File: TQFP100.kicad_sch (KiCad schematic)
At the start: 5 parts, among them IC1 100-PQFP, J1 Conn_02x15_Counter_Clockwise, J2 Conn_02x10_Odd_Even_MountingP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, J3 Conn_02x15_Counter_Clockwise, J4 Conn_02x10_Odd_Even_MountingP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

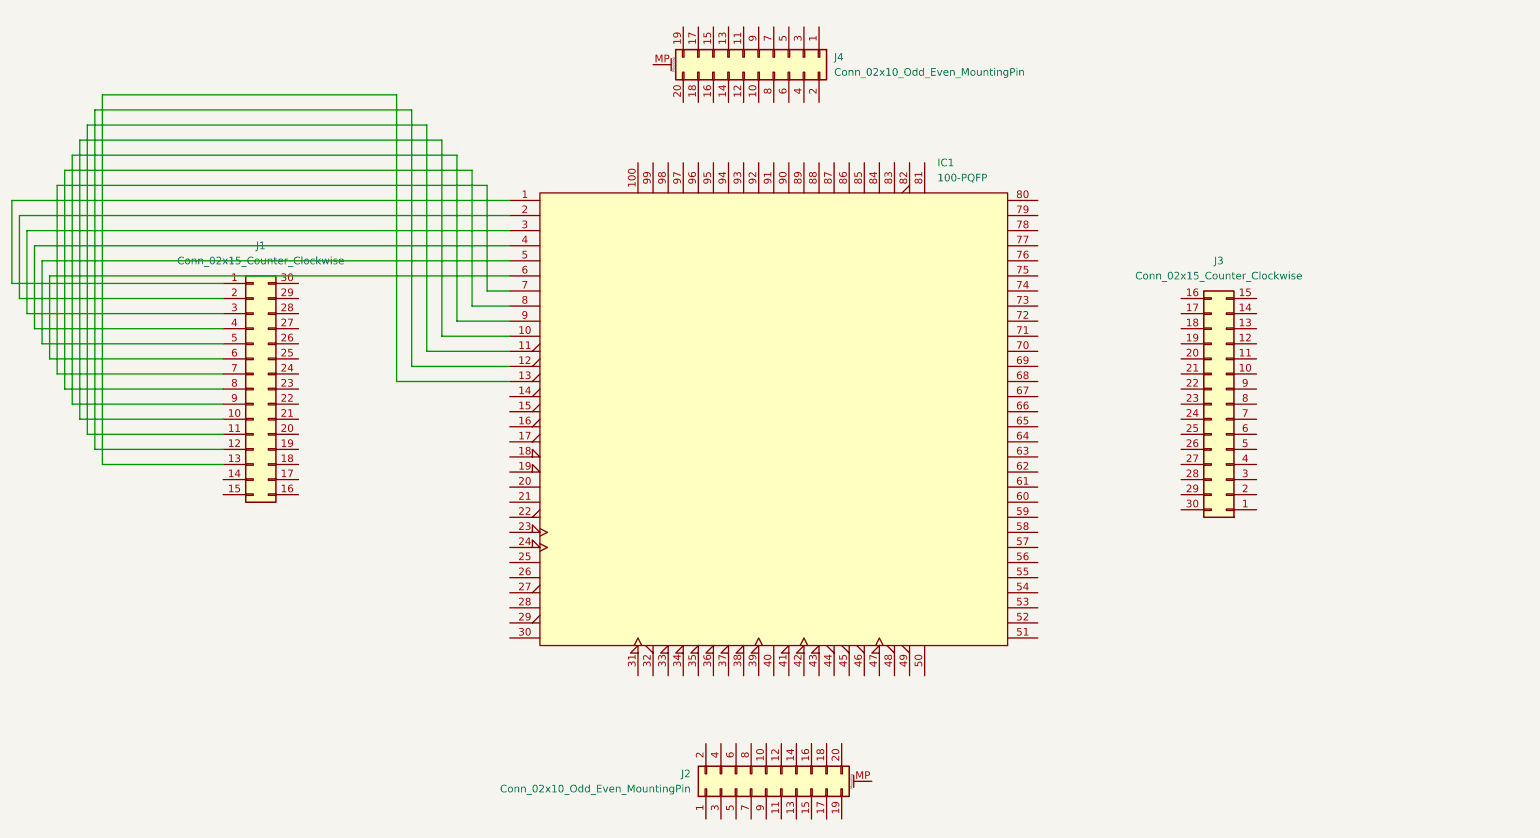
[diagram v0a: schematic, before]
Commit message: Corrected pinheader size
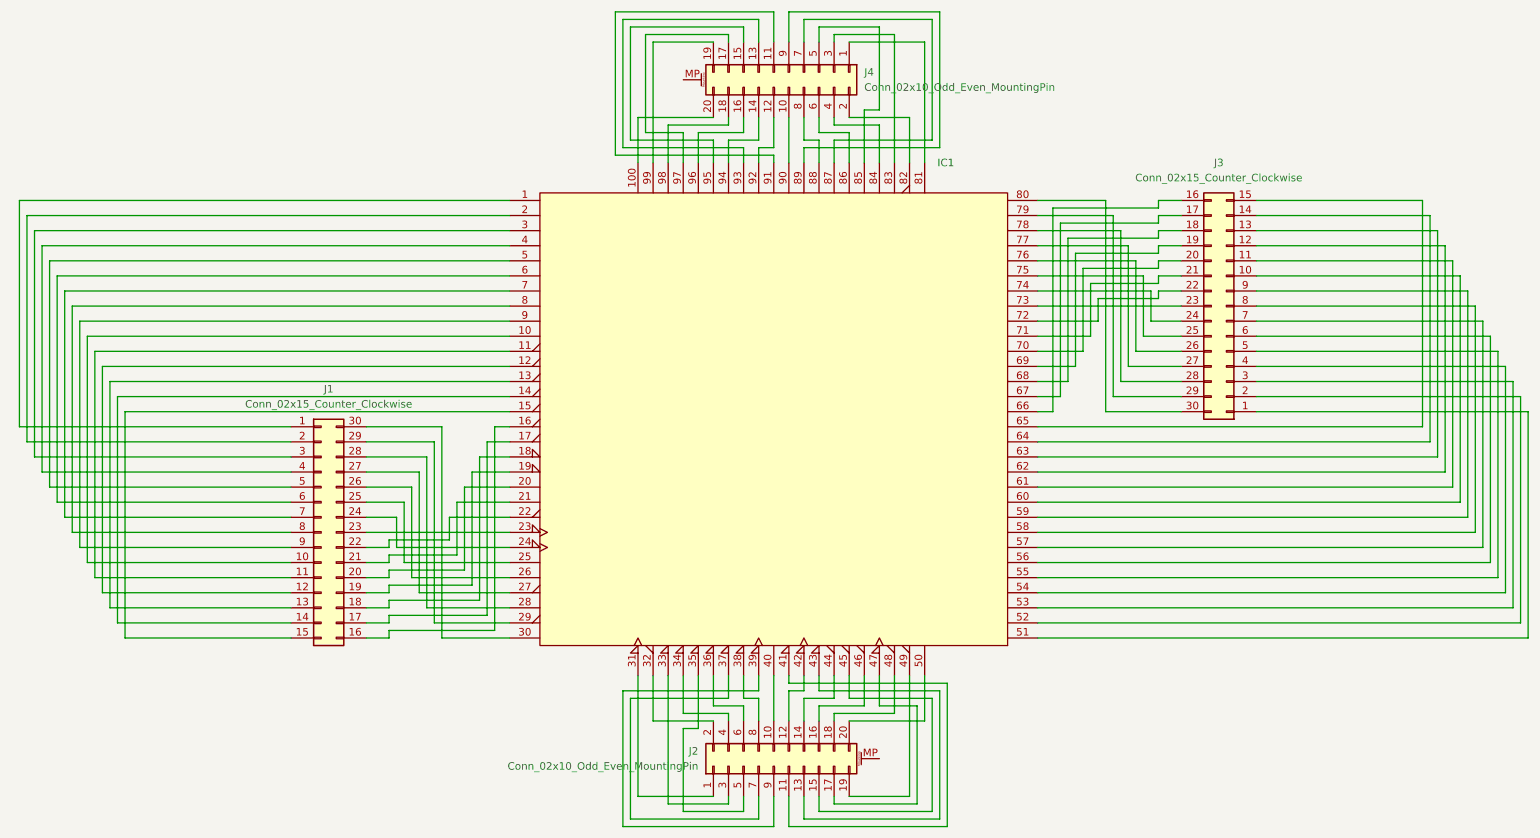
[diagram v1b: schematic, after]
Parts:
- J1, J3: footprint Connector_PinHeader_1.00mm:PinHeader_2x15_P1.00mm_Vertical -> Connector_PinHeader_2.54mm:PinHeader_2x15_P2.54mm_Vertical
- J2, J4: footprint Connector_PinHeader_1.00mm:PinHeader_2x10_P1.00mm_Vertical -> Connector_PinHeader_2.54mm:PinHeader_2x10_P2.54mm_Vertical
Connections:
- net at J4.1 (Pin_1): now also IC1.81 (A22)
- net at J4.10 (Pin_10): now also IC1.90 (VDD_8)
- net at J4.11 (Pin_11): now also IC1.91 (A15)
- net at J4.12 (Pin_12): now also IC1.92 (A14)
- net at J4.13 (Pin_13): now also IC1.93 (A13)
- net at J4.14 (Pin_14): now also IC1.94 (A12)
- net at J4.15 (Pin_15): now also IC1.95 (A11)
- net at J4.16 (Pin_16): now also IC1.96 (A10)
- net at J4.17 (Pin_17): now also IC1.97 (A09)
- net at J4.18 (Pin_18): now also IC1.98 (A08)
- net at J4.19 (Pin_19): now also IC1.99 (A07)
- net at J4.2 (Pin_2): now also IC1.82 (A21)
- net at J4.20 (Pin_20): now also IC1.100 (A06)
- net at J4.3 (Pin_3): now also IC1.83 (A20)
- net at J4.4 (Pin_4): now also IC1.84 (A19)
- net at J4.5 (Pin_5): now also IC1.85 (A18)
- net at J4.6 (Pin_6): now also IC1.86 (A17)
- net at J4.7 (Pin_7): now also IC1.87 (A16)
- net at J4.8 (Pin_8): now also IC1.88 (VDD_7)
- net at J4.9 (Pin_9): now also IC1.89 (VSS_8)
- net at J2.1 (Pin_1): now also IC1.31 (~{INTAK})
- net at J2.10 (Pin_10): now also IC1.40 (CLKSEL)
- net at J2.11 (Pin_11): now also IC1.41 (~{HALT})
- net at J2.12 (Pin_12): now also IC1.42 (~{STNBY})
- net at J2.13 (Pin_13): now also IC1.43 (~{EV})
- net at J2.14 (Pin_14): now also IC1.44 (~{UMCS})
- net at J2.15 (Pin_15): now also IC1.45 (~{MCS3})
- net at J2.16 (Pin_16): now also IC1.46 (~{MCS2})
- net at J2.17 (Pin_17): now also IC1.47 (~{MCS1})
- net at J2.18 (Pin_18): now also IC1.48 (~{MCS0})
- net at J2.19 (Pin_19): now also IC1.49 (~{LMCS})
- net at J2.2 (Pin_2): now also IC1.32 (~{BACK})
- net at J2.20 (Pin_20): now also IC1.50 (VDD_4)
- net at J2.3 (Pin_3): now also IC1.33 (~{BREQ})
- net at J2.4 (Pin_4): now also IC1.34 (~{RESET})
- net at J2.5 (Pin_5): now also IC1.35 (~{INT3})
- net at J2.6 (Pin_6): now also IC1.36 (~{INT2})
- net at J2.7 (Pin_7): now also IC1.37 (~{INT1})
- net at J2.8 (Pin_8): now also IC1.38 (~{INT0})
- net at J2.9 (Pin_9): now also IC1.39 (~{NMI})
- net at IC1.14 (~{BHEN}): now also J1.14 (Pin_14)
- net at IC1.15 (~{BLEN}): now also J1.15 (Pin_15)
- net at IC1.16 (~{MRD}): now also J1.16 (Pin_16)
- net at IC1.17 (~{MWR}): now also J1.17 (Pin_17)
- net at IC1.18 (~{MSIZE}): now also J1.18 (Pin_18)
- net at IC1.19 (~{WAIT}): now also J1.19 (Pin_19)
- net at IC1.20 (BUSCLK): now also J1.20 (Pin_20)
- net at IC1.21 (IOCLK): now also J1.21 (Pin_21)
- net at IC1.22 (~{M1}): now also J1.22 (Pin_22)
- net at IC1.23 (~{IORQ}): now also J1.23 (Pin_23)
- net at IC1.24 (~{IORD}): now also J1.24 (Pin_24)
- net at IC1.25 (CLKI): now also J1.25 (Pin_25)
- net at IC1.26 (CLKO): now also J1.26 (Pin_26)
- net at IC1.27 (~{IOWR}): now also J1.27 (Pin_27)
- net at IC1.28 (VSS_3): now also J1.28 (Pin_28)
- net at IC1.29 (~{UMCS}): now also J1.29 (Pin_29)
- net at IC1.30 (VSS_4): now also J1.30 (Pin_30)
- net at IC1.51 (VSS_5): now also J3.1 (Pin_1)
- net at IC1.52 (VDD_5): now also J3.2 (Pin_2)
- net at IC1.53 (D15): now also J3.3 (Pin_3)
- net at IC1.54 (D14): now also J3.4 (Pin_4)
- net at IC1.55 (D13): now also J3.5 (Pin_5)
- net at IC1.56 (D12): now also J3.6 (Pin_6)
- net at IC1.57 (D11): now also J3.7 (Pin_7)
- net at IC1.58 (D10): now also J3.8 (Pin_8)
- net at IC1.59 (D09): now also J3.9 (Pin_9)
- net at IC1.60 (D08): now also J3.10 (Pin_10)
- net at IC1.61 (D07): now also J3.11 (Pin_11)
- net at IC1.62 (D06): now also J3.12 (Pin_12)
- net at IC1.63 (D05): now also J3.13 (Pin_13)
- net at IC1.64 (D04): now also J3.14 (Pin_14)
- net at IC1.65 (D03): now also J3.15 (Pin_15)
- net at IC1.66 (D02): now also J3.16 (Pin_16)
- net at IC1.67 (D01): now also J3.17 (Pin_17)
- net at IC1.68 (D00): now also J3.18 (Pin_18)
- net at IC1.69 (VSS_6): now also J3.19 (Pin_19)
- net at IC1.70 (VDD_6): now also J3.20 (Pin_20)
- net at IC1.71 (VSS_7): now also J3.21 (Pin_21)
- net at IC1.72 (A31): now also J3.22 (Pin_22)
- net at IC1.73 (A30): now also J3.23 (Pin_23)
- net at IC1.74 (A29): now also J3.24 (Pin_24)
- net at IC1.75 (A28): now also J3.25 (Pin_25)
- net at IC1.76 (A27): now also J3.26 (Pin_26)
- net at IC1.77 (A26): now also J3.27 (Pin_27)
- net at IC1.78 (A25): now also J3.28 (Pin_28)
- net at IC1.79 (A24): now also J3.29 (Pin_29)
- net at IC1.80 (A23): now also J3.30 (Pin_30)
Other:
- moved on the sheet: J1, J2, J3, J4

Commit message: Fixed the whole board, with correct names
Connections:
- no-connect marks 0 -> 1
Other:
- title: TQFP-100 adapter board -> PQFP-100 adapter board
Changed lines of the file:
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@@
 	(paper "A4")
 	(title_block
-		(title "TQFP-100 adapter board")
+		(title "PQFP-100 adapter board")
 		(date "2025-02-25")
 		(rev "1")
@@
 		(comment 1 "Prototype board series 1")
 	)
+	(no_connect
+		(at 88.9 -173.99)
+	)
 	(wire
